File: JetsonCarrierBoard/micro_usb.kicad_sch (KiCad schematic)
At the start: 0 parts

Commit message: Micro USB B 2.0 Basic Wiring
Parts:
- added C?: 0.1u, symbol Device:C
- added C?: 4.7u, symbol Device:C
- added D? (x3): D_TVS, symbol Device:D_TVS
- added J?: USB_B_Micro, symbol Connector:USB_B_Micro
- added Q?: DMN24H3D5L, Package_TO_SOT_SMD:SOT-23, symbol Transistor_FET:DMN24H3D5L
- added R?: 0, symbol Device:R
- added R?: 1M, symbol Device:R
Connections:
- new net: Q?.1 (G), R?.2, R?.2
- new net: C?.1, D?.2 (A2), J?.1 (VBUS), R?.1
- new net GND: C?.2, C?.2, D?.1 (A1), D?.1 (A1), D?.1 (A1), J?.5 (GND), J?.6 (Shield), Q?.2 (S), R?.1
- new net USB0_VBUS_DET*: Q?.3 (D)
- new net USB_M_DN: D?.2 (A2), J?.2 (D-)
- new net USB_M_DP: C?.1, D?.2 (A2), J?.3 (D+)
- no-connect marks 0 -> 1

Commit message: Adding more Title block info and changing main hierarchical page layout
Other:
- title: (none) -> Micro USB B 2.0
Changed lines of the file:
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@@
 (kicad_sch (version 20211123) (generator eeschema)
   (paper "A4")
+  (title_block
+    (title "Micro USB B 2.0")
+    (date "2022-09-18")
+    (rev "1.0")
+  )
   (junction (at 121.92 83.82) (diameter 0) (color 0 0 0 0)
   )

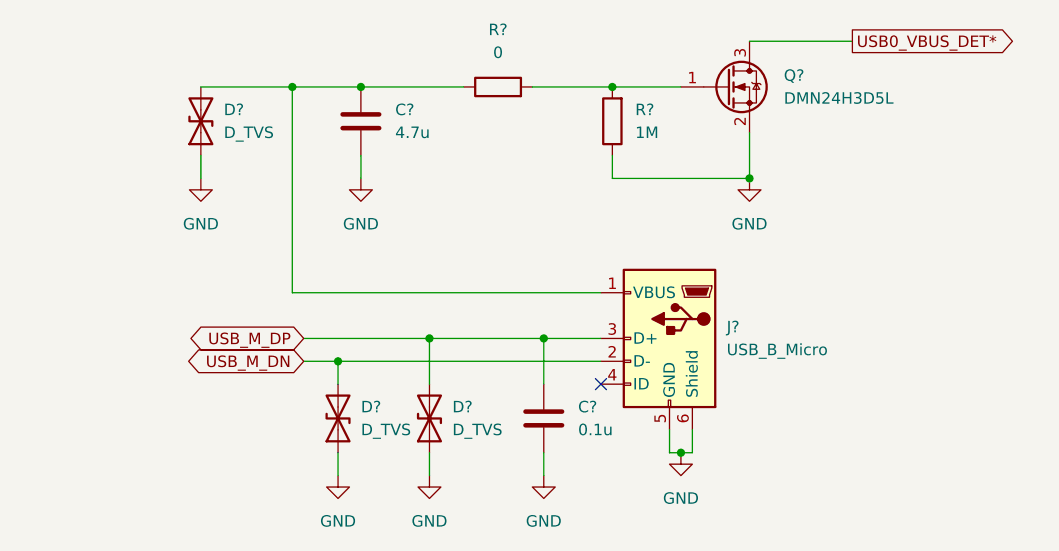
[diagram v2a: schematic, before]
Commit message: Improvement list, fixes, and readability improvements
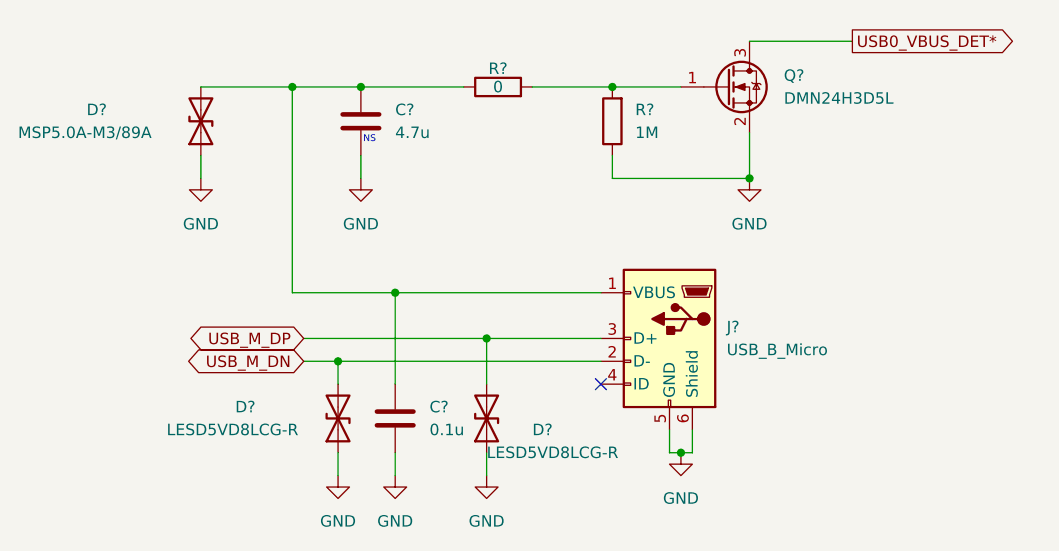
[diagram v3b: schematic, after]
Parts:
- removed C?: 0.1u, symbol Device:C
- added C?: 0.1u, symbol Device:C
- D? (x2): value D_TVS -> LESD5VD8LCG-R
- D?: value D_TVS -> MSP5.0A-M3/89A
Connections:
- net GND: now also C?.2
- net at C?.1, D?.2 (A2), J?.1 (VBUS)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: now also C?.1
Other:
- note added: "NS"
- title: Micro USB B 2.0 -> Micro USB (DEVICE MODE ONLY)
- moved on the sheet: D?
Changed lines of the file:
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@@
   (paper "A4")
   (title_block
-    (title "Micro USB B 2.0")
+    (title "Micro USB (DEVICE MODE ONLY)")
     (date "2022-09-18")
     (rev "1.0")
@@
   (junction (at 129.54 83.82) (diameter 0) (color 0 0 0 0)
   )
-  (junction (at 149.86 111.76) (diameter 0) (color 0 0 0 0)
+  (junction (at 143.51 111.76) (diameter 0) (color 0 0 0 0)
   )
   (junction (at 165.1 124.46) (diameter 0) (color 0 0 0 0)
   )
-  (junction (at 137.16 111.76) (diameter 0) (color 0 0 0 0)
-  )
   (junction (at 127 114.3) (diameter 0) (color 0 0 0 0)
   )
@@
   (junction (at 157.48 83.82) (diameter 0) (color 0 0 0 0)
   )
+  (junction (at 133.35 106.68) (diameter 0) (color 0 0 0 0)
+  )
   (no_connect (at 156.21 116.84))
-  (wire (pts (xy 156.21 106.68) (xy 121.92 106.68))
-    (stroke (width 0) (type default) (color 0 0 0 0))
-  )
-  (wire (pts (xy 123.19 111.76) (xy 137.16 111.76))
-    (stroke (width 0) (type default) (color 0 0 0 0))
-  )
-  (wire (pts (xy 149.86 124.46) (xy 149.86 127))
+  (wire (pts (xy 123.19 111.76) (xy 143.51 111.76))
     (stroke (width 0) (type default) (color 0 0 0 0))
   )
@@
     (stroke (width 0) (type default) (color 0 0 0 0))
   )
-  (wire (pts (xy 149.86 111.76) (xy 149.86 116.84))
-    (stroke (width 0) (type default) (color 0 0 0 0))
-  )
-  (wire (pts (xy 149.86 111.76) (xy 156.21 111.76))
+  (wire (pts (xy 133.35 124.46) (xy 133.35 127))
+    (stroke (width 0) (type default) (color 0 0 0 0))
+  )
+  (wire (pts (xy 133.35 106.68) (xy 156.21 106.68))
     (stroke (width 0) (type default) (color 0 0 0 0))
   )
@@
     (stroke (width 0) (type default) (color 0 0 0 0))
   )
+  (wire (pts (xy 143.51 111.76) (xy 143.51 116.84))
+    (stroke (width 0) (type default) (color 0 0 0 0))
+  )
   (wire (pts (xy 127 114.3) (xy 127 116.84))
     (stroke (width 0) (type default) (color 0 0 0 0))
@@
     (stroke (width 0) (type default) (color 0 0 0 0))
   )
-  (wire (pts (xy 137.16 111.76) (xy 149.86 111.76))
-    (stroke (width 0) (type default) (color 0 0 0 0))
-  )
   (wire (pts (xy 111.76 83.82) (xy 121.92 83.82))
     (stroke (width 0) (type default) (color 0 0 0 0))
@@
     (stroke (width 0) (type default) (color 0 0 0 0))
   )
-  (wire (pts (xy 137.16 124.46) (xy 137.16 127))
-    (stroke (width 0) (type default) (color 0 0 0 0))
-  )
-  (wire (pts (xy 137.16 111.76) (xy 137.16 116.84))
+  (wire (pts (xy 143.51 124.46) (xy 143.51 127))
+    (stroke (width 0) (type default) (color 0 0 0 0))
+  )
+  (wire (pts (xy 143.51 111.76) (xy 156.21 111.76))
     (stroke (width 0) (type default) (color 0 0 0 0))
   )
   (wire (pts (xy 111.76 91.44) (xy 111.76 93.98))
     (stroke (width 0) (type default) (color 0 0 0 0))
+  )
+  (wire (pts (xy 121.92 106.68) (xy 133.35 106.68))
+    (stroke (width 0) (type default) (color 0 0 0 0))
+  )
+  (wire (pts (xy 133.35 106.68) (xy 133.35 116.84))
+    (stroke (width 0) (type default) (color 0 0 0 0))
+  )
+  (text "NS" (at 129.794 90.17 0)
+    (effects (font (size 0.75 0.75)) (justify left bottom))
   )
   (global_label "USB_M_DN" (shape bidirectional) (at 123.19 114.3 180) (fields_autoplaced)
@@
     (pin "3")
   )
-  (symbol (lib_id "Device:D_TVS") (at 137.16 120.65 90) (unit 1)
-    (in_bom yes) (on_board yes) (fields_autoplaced)
-    (property "Reference" "D?" (id 0) (at 139.7 119.3799 90)
-      (effects (font (size 1.27 1.27)) (justify right))
-    )
-    (property "Value" "D_TVS" (id 1) (at 139.7 121.9199 90)
-      (effects (font (size 1.27 1.27)) (justify right))
-    )
-    (property "Footprint" "" (id 2) (at 137.16 120.65 0)
-      (effects (font (size 1.27 1.27)) hide)
-    )
-    (property "Datasheet" "~" (id 3) (at 137.16 120.65 0)
+  (symbol (lib_id "Device:D_TVS") (at 143.51 120.65 90) (unit 1)
+    (in_bom yes) (on_board yes)
+    (property "Reference" "D?" (id 0) (at 148.59 121.92 90)
+      (effects (font (size 1.27 1.27)) (justify right))
+    )
+    (property "Value" "LESD5VD8LCG-R" (id 1) (at 143.51 124.46 90)
+      (effects (font (size 1.27 1.27)) (justify right))
+    )
+    (property "Footprint" "" (id 2) (at 143.51 120.65 0)
+      (effects (font (size 1.27 1.27)) hide)
+    )
+    (property "Datasheet" "~" (id 3) (at 143.51 120.65 0)
       (effects (font (size 1.27 1.27)) hide)
     )
@@
   )
   (symbol (lib_id "Device:D_TVS") (at 111.76 87.63 90) (unit 1)
-    (in_bom yes) (on_board yes) (fields_autoplaced)
-    (property "Reference" "D?" (id 0) (at 114.3 86.3599 90)
-      (effects (font (size 1.27 1.27)) (justify right))
-    )
-    (property "Value" "D_TVS" (id 1) (at 114.3 88.8999 90)
+    (in_bom yes) (on_board yes)
+    (property "Reference" "D?" (id 0) (at 99.06 86.36 90)
+      (effects (font (size 1.27 1.27)) (justify right))
+    )
+    (property "Value" "MSP5.0A-M3/89A" (id 1) (at 91.44 88.9 90)
       (effects (font (size 1.27 1.27)) (justify right))
     )
@@
     (pin "2")
   )
-  (symbol (lib_id "Device:C") (at 149.86 120.65 0) (unit 1)
-    (in_bom yes) (on_board yes) (fields_autoplaced)
-    (property "Reference" "C?" (id 0) (at 153.67 119.3799 0)
-      (effects (font (size 1.27 1.27)) (justify left))
-    )
-    (property "Value" "0.1u" (id 1) (at 153.67 121.9199 0)
-      (effects (font (size 1.27 1.27)) (justify left))
-    )
-    (property "Footprint" "" (id 2) (at 150.8252 124.46 0)
-      (effects (font (size 1.27 1.27)) hide)
-    )
-    (property "Datasheet" "~" (id 3) (at 149.86 120.65 0)
+  (symbol (lib_id "Device:C") (at 133.35 120.65 0) (unit 1)
+    (in_bom yes) (on_board yes) (fields_autoplaced)
+    (property "Reference" "C?" (id 0) (at 137.16 119.3799 0)
+      (effects (font (size 1.27 1.27)) (justify left))
+    )
+    (property "Value" "0.1u" (id 1) (at 137.16 121.9199 0)
+      (effects (font (size 1.27 1.27)) (justify left))
+    )
+    (property "Footprint" "" (id 2) (at 134.3152 124.46 0)
+      (effects (font (size 1.27 1.27)) hide)
+    )
+    (property "Datasheet" "~" (id 3) (at 133.35 120.65 0)
       (effects (font (size 1.27 1.27)) hide)
     )
@@
   )
   (symbol (lib_id "Device:R") (at 144.78 83.82 90) (unit 1)
-    (in_bom yes) (on_board yes) (fields_autoplaced)
-    (property "Reference" "R?" (id 0) (at 144.78 77.47 90))
-    (property "Value" "0" (id 1) (at 144.78 80.01 90))
+    (in_bom yes) (on_board yes)
+    (property "Reference" "R?" (id 0) (at 144.78 81.788 90))
+    (property "Value" "0" (id 1) (at 144.78 83.82 90))
     (property "Footprint" "" (id 2) (at 144.78 85.598 90)
       (effects (font (size 1.27 1.27)) hide)
@@
     (pin "1")
     (pin "2")
+  )
+  (symbol (lib_id "power:GND") (at 133.35 127 0) (unit 1)
+    (in_bom yes) (on_board yes) (fields_autoplaced)
+    (property "Reference" "#PWR?" (id 0) (at 133.35 133.35 0)
+      (effects (font (size 1.27 1.27)) hide)
+    )
+    (property "Value" "GND" (id 1) (at 133.35 132.08 0))
+    (property "Footprint" "" (id 2) (at 133.35 127 0)
+      (effects (font (size 1.27 1.27)) hide)
+    )
+    (property "Datasheet" "" (id 3) (at 133.35 127 0)
+      (effects (font (size 1.27 1.27)) hide)
+    )
+    (pin "1")
   )
   (symbol (lib_id "Device:R") (at 157.48 87.63 180) (unit 1)
@@
   )
   (symbol (lib_id "Device:D_TVS") (at 127 120.65 90) (unit 1)
-    (in_bom yes) (on_board yes) (fields_autoplaced)
-    (property "Reference" "D?" (id 0) (at 129.54 119.3799 90)
-      (effects (font (size 1.27 1.27)) (justify right))
-    )
-    (property "Value" "D_TVS" (id 1) (at 129.54 121.9199 90)
+    (in_bom yes) (on_board yes)
+    (property "Reference" "D?" (id 0) (at 115.57 119.38 90)
+      (effects (font (size 1.27 1.27)) (justify right))
+    )
+    (property "Value" "LESD5VD8LCG-R" (id 1) (at 107.95 121.92 90)
       (effects (font (size 1.27 1.27)) (justify right))
     )
@@
     (pin "1")
   )
-  (symbol (lib_id "power:GND") (at 149.86 127 0) (unit 1)
-    (in_bom yes) (on_board yes) (fields_autoplaced)
-    (property "Reference" "#PWR?" (id 0) (at 149.86 133.35 0)
-      (effects (font (size 1.27 1.27)) hide)
-    )
-    (property "Value" "GND" (id 1) (at 149.86 132.08 0))
-    (property "Footprint" "" (id 2) (at 149.86 127 0)
-      (effects (font (size 1.27 1.27)) hide)
-    )
-    (property "Datasheet" "" (id 3) (at 149.86 127 0)
-      (effects (font (size 1.27 1.27)) hide)
-    )
-    (pin "1")
-  )
   (symbol (lib_id "power:GND") (at 127 127 0) (unit 1)
     (in_bom yes) (on_board yes) (fields_autoplaced)
@@
     (pin "1")
   )
-  (symbol (lib_id "power:GND") (at 137.16 127 0) (unit 1)
-    (in_bom yes) (on_board yes) (fields_autoplaced)
-    (property "Reference" "#PWR?" (id 0) (at 137.16 133.35 0)
-      (effects (font (size 1.27 1.27)) hide)
-    )
-    (property "Value" "GND" (id 1) (at 137.16 132.08 0))
-    (property "Footprint" "" (id 2) (at 137.16 127 0)
-      (effects (font (size 1.27 1.27)) hide)
-    )
-    (property "Datasheet" "" (id 3) (at 137.16 127 0)
-      (effects (font (size 1.27 1.27)) hide)
-    )
+  (symbol (lib_id "power:GND") (at 143.51 127 0) (unit 1)
+    (in_bom yes) (on_board yes) (fields_autoplaced)
+    (property "Reference" "#PWR?" (id 0) (at 143.51 133.35 0)
+      (effects (font (size 1.27 1.27)) hide)
+    )
+    (property "Value" "GND" (id 1) (at 143.51 132.08 0))
+    (property "Footprint" "" (id 2) (at 143.51 127 0)
+      (effects (font (size 1.27 1.27)) hide)
+    )
+    (property "Datasheet" "" (id 3) (at 143.51 127 0)
+      (effects (font (size 1.27 1.27)) hide)
+    )
